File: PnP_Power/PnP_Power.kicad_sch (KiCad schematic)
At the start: 64 parts, among them J1 Barrel Jack 5mm x 2.5mm 54-00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, U7 VNH5019A-E, U8 LMS78_05-2.0R, U9 SN74LVC2G04DBVR

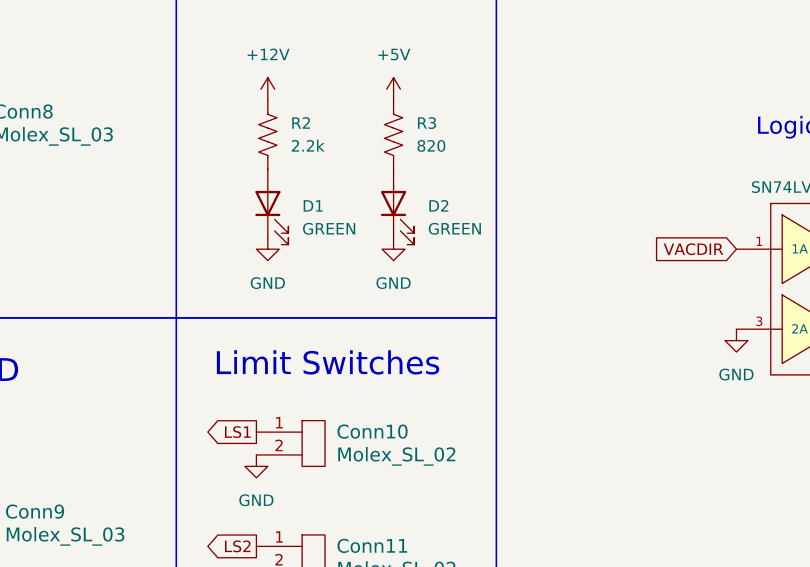
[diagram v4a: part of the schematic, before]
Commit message: Routed and Labeled layout
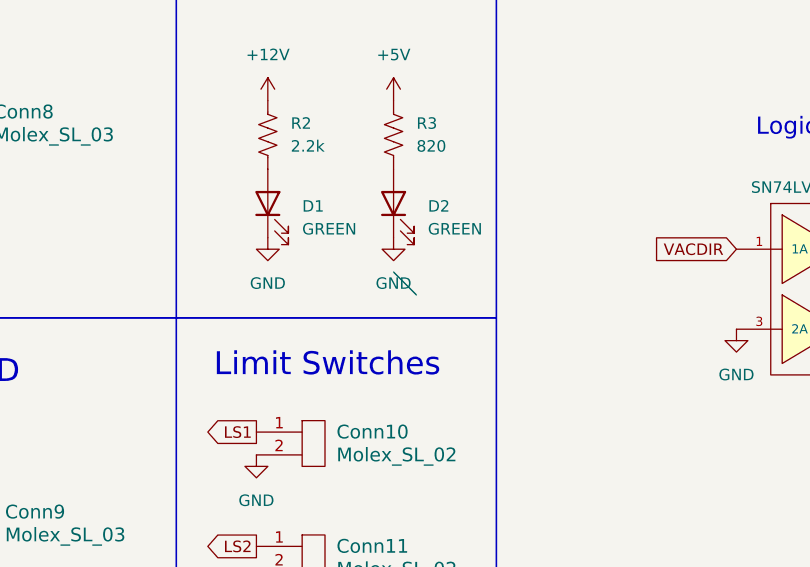
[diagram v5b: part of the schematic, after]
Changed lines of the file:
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@@
 		(at 312.42 46.99)
+	)
+	(bus_entry
+		(at 87.63 187.96)
+		(size 2.54 2.54)
+		(stroke
+			(width 0)
+			(type default)
+		)
 	)
 	(wire

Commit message: Many things
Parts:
- removed JP1, JP10, JP11, JP12, JP13, JP14, JP15, JP16, JP17, JP18, JP2, JP3, JP4, JP5, JP6, JP7, JP8, JP9: Jumper_2_Bridged, Connector_PinHeader_2.54mm:PinHeader_1x02_P2.54mm_Vertical, symbol Jumper:Jumper_2_Bridged
- added C10, C11, C12, C13, C14, C15, C16, C17, C18, C19, C20, C21: 0.1uF, Capacitor_SMD:C_0603_1608Metric_Pad1.08x0.95mm_HandSolder, symbol Device:C
- added Conn16, Conn17, Conn18, Conn19, Conn20, Conn21: Molex_SL_02, MRDT_Connectors:MOLEX_SL_02_Horizontal, symbol MRDT_Connectors:Molex_SL_02
- added J2, J3, J4, J5, J6, J7: Conn_02x03_Odd_Even, Connector_PinHeader_2.54mm:PinHeader_2x03_P2.54mm_Vertical, symbol Connector_Generic:Conn_02x03_Odd_Even
- added R1, R10, R11, R12, R13, R14, R15, R16, R17, R4, R5, R9: 1k, Resistor_SMD:R_0603_1608Metric_Pad0.98x0.95mm_HandSolder, symbol Device:R_US
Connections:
- net +5V: now also J2.2 (Pin_2), J2.4 (Pin_4), J2.6 (Pin_6), J3.2 (Pin_2), J3.4 (Pin_4), J3.6 (Pin_6), J4.2 (Pin_2), J4.4 (Pin_4), J4.6 (Pin_6), J5.2 (Pin_2), J5.4 (Pin_4), J5.6 (Pin_6), J6.2 (Pin_2), J6.4 (Pin_4), J6.6 (Pin_6), J7.2 (Pin_2), J7.4 (Pin_4), J7.6 (Pin_6); no longer U1.11 (Sleep), U1.12 (Reset), U2.11 (Sleep), U2.12 (Reset), U3.11 (Sleep), U3.12 (Reset), U4.11 (Sleep), U4.12 (Reset), U5.11 (Sleep), U5.12 (Reset), U6.11 (Sleep), U6.12 (Reset)
- net GND: now also C10.2, C11.2, C12.2, C13.2, C14.2, C15.2, C16.2, C17.2, C18.2, C19.2, C20.2, C21.2, Conn16.2, Conn17.2, Conn18.2, Conn19.2, Conn20.2, Conn21.2
- net LS1: now also A1.3, R1.1; no longer A1.23, Conn10.1
- net LS2: now also A1.2, R4.1; no longer A1.25, Conn11.1
- net LS3: now also A1.14, R5.1; no longer A1.27, Conn12.1
- net LS4: now also A1.15, R9.1; no longer A1.29, Conn13.1
- net LS5: now also A1.18, R10.1; no longer A1.31, Conn14.1
- net LS6: now also A1.19, R11.1; no longer A1.33, Conn15.1
- net at U1.15 (MS1): now also J7.1 (Pin_1)
- net at U4.13 (MS3): now also J4.5 (Pin_5)
- net at U4.14 (MS2): now also J4.3 (Pin_3)
- net at U4.15 (MS1): now also J4.1 (Pin_1)
- net at U3.15 (MS1): now also J5.1 (Pin_1)
- net at U2.14 (MS2): now also J6.3 (Pin_3)
- net at U1.14 (MS2): now also J7.3 (Pin_3)
- net at U5.15 (MS1): now also J3.1 (Pin_1)
- net at U1.13 (MS3): now also J7.5 (Pin_5)
- net at U6.15 (MS1): now also J2.1 (Pin_1)
- net at U5.14 (MS2): now also J3.3 (Pin_3)
- net at U5.13 (MS3): now also J3.5 (Pin_5)
- net at U3.13 (MS3): now also J5.5 (Pin_5)
- net at U3.14 (MS2): now also J5.3 (Pin_3)
- net at U2.13 (MS3): now also J6.5 (Pin_5)
- net at U2.15 (MS1): now also J6.1 (Pin_1)
- net at U6.13 (MS3): now also J2.5 (Pin_5)
- net at U6.14 (MS2): now also J2.3 (Pin_3)
- net LS8: now reaches A1.40
- net LS8: now also R13.1
- net LS7: now reaches A1.42
- net LS7: now also R12.1
- net LS9: now reaches A1.44
- net LS9: now also R14.1
- net LS11: now reaches A1.AD3
- net LS11: now also R16.1
- net LS12: now reaches A1.AD4
- net LS12: now also R17.1
- net LS10: now reaches A1.AD5
- net LS10: now also R15.1
- new net: C11.1, Conn11.1, R4.2
- new net: C13.1, Conn13.1, R9.2
- new net: C17.1, Conn17.1, R13.2
- new net: C19.1, Conn19.1, R15.2
- new net: C21.1, Conn21.1, R17.2
- new net: C10.1, Conn10.1, R1.2
- new net: U4.11 (Sleep), U4.12 (Reset)
- new net: C12.1, Conn12.1, R5.2
- new net: C14.1, Conn14.1, R10.2
- new net: C15.1, Conn15.1, R11.2
- new net: C18.1, Conn18.1, R14.2
- new net: C16.1, Conn16.1, R12.2
- new net: C20.1, Conn20.1, R16.2
- new net: U2.11 (Sleep), U2.12 (Reset)
- new net: U3.11 (Sleep), U3.12 (Reset)
- new net: U5.11 (Sleep), U5.12 (Reset)
- new net: U6.11 (Sleep), U6.12 (Reset)
- new net: U1.11 (Sleep), U1.12 (Reset)
- no-connect marks 7 -> 39
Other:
- moved on the sheet: Conn10, Conn11, Conn12, Conn13, Conn14, Conn15

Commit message: Some changes from doc
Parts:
- added J8, J9: Conn_01x03_Pin, Connector_PinHeader_2.54mm:PinHeader_1x03_P2.54mm_Vertical, symbol Connector:Conn_01x03_Pin
- added Q1, Q2: PMOS, Package_TO_SOT_SMD:SOT-23, symbol Simulation_SPICE:PMOS
- added R18, R19: 1k, Resistor_SMD:R_0603_1608Metric_Pad0.98x0.95mm_HandSolder, symbol Device:R_US
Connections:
- net +5V: now also J8.1 (Pin_1), J9.1 (Pin_1), Q1.2 (S), Q2.2 (S), R18.1, R19.1; no longer Conn8.2, Conn9.2
- net LED1: now also Q2.1 (G), R18.2
- net LED2: now also Q1.1 (G), R19.2
- net LS1 renamed X_LIM_MIN
- net LS10 renamed B_LIM_MAX
- net LS11 renamed C_LIM_MIN
- net LS12 renamed C_LIM_MAX
- net LS2 renamed X_LIM_MAX
- net LS3 renamed Y_LIM_MIN
- net LS4 renamed Y_LIM_MAX
- net LS5 renamed Z_LIM_MIN
- net LS6 renamed Z_LIM_MAX
- net LS7 renamed A_LIM_MIN
- net LS8 renamed A_LIM_MAX
- net LS9 renamed B_LIM_MIN
- new net: Conn8.2, J9.2 (Pin_2)
- new net: Conn9.2, J8.2 (Pin_2)
- new net: J9.3 (Pin_3), Q2.3 (D)
- new net: J8.3 (Pin_3), Q1.3 (D)
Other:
- note added: "LED"
- note added: "NEMA 17 B Axis"
- note added: "NEMA 17 X1 Axis"
- note added: "NEMA 17 X2 Axis"
- note added: "NEMA 17 Y Axis"
- note removed: "NEMA 17 COMP FEED"
- note removed: "NEMA 17 X Axis"
- note removed: "NEMA 17 Y Axis 1"
- note removed: "NEMA 17 Y Axis 2"
- note removed: "White LED"
- moved on the sheet: Conn9
